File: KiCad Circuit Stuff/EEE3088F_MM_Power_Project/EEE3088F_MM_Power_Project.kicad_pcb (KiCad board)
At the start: 2 copper layers, 60 parts, among them J1 Conn_01x02, J2 Conn_02x16_Odd_Even, U1 MT3608, U2 INA219AIDCNR, U3 AMS1117-3.3, U4 TPS5430DDAR, U5 TP4056, U6 TS5A3159DCKR

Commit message: Connected All circuits, Ready for pcb design
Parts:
- added C13: 1uF, Capacitor_SMD:C_0402_1005Metric_Pad0.74x0.62mm_HandSolder, F.Cu at (167.0, 39.4)
- added C14: 10uF, Capacitor_SMD:C_0603_1608Metric_Pad1.08x0.95mm_HandSolder, F.Cu at (167.6, 53.5)
- added C17: 10uF, Capacitor_SMD:C_0603_1608Metric_Pad1.08x0.95mm_HandSolder, F.Cu at (167.6, 56.0)
- added C18: 220uF, Capacitor_SMD:C_Elec_6.3x7.7, F.Cu at (160.5, 42.5)
- added C19: 220uF, Capacitor_SMD:C_Elec_6.3x7.7, F.Cu at (160.5, 50.6)
- added C20: 220uF, Capacitor_SMD:C_Elec_6.3x7.7, F.Cu at (160.5, 58.8)
- added C21: 220uF, Capacitor_SMD:C_Elec_6.3x7.7, F.Cu at (160.5, 67.0)
- added C22: 100nF, Capacitor_SMD:C_0402_1005Metric_Pad0.74x0.62mm_HandSolder, F.Cu at (167.0, 41.4)
- added C23: 100nF, Capacitor_SMD:C_0402_1005Metric_Pad0.74x0.62mm_HandSolder, F.Cu at (167.0, 43.4)
- added C24: 220uF, Capacitor_SMD:C_Elec_6.3x7.7, F.Cu at (160.5, 75.1)
- added C25: 220uF, Capacitor_SMD:C_Elec_6.3x7.7, F.Cu at (160.5, 83.2)
- added C26: 100nF, Capacitor_SMD:C_0402_1005Metric_Pad0.74x0.62mm_HandSolder, F.Cu at (167.0, 45.3)
- added C27: 1uF, Capacitor_SMD:C_0402_1005Metric_Pad0.74x0.62mm_HandSolder, F.Cu at (167.0, 47.3)
- added C28: 1uF, Capacitor_SMD:C_0402_1005Metric_Pad0.74x0.62mm_HandSolder, F.Cu at (167.0, 49.3)
- added C29: 1uF, Capacitor_SMD:C_0402_1005Metric_Pad0.74x0.62mm_HandSolder, F.Cu at (167.0, 51.2)
- added C30: 220uF, Capacitor_SMD:C_Elec_6.3x7.7, F.Cu at (180.7, 43.0)
- added C31: 220uF, Capacitor_SMD:C_Elec_6.3x7.7, F.Cu at (180.7, 51.2)
- added C32: 100nF, Capacitor_SMD:C_0402_1005Metric_Pad0.74x0.62mm_HandSolder, F.Cu at (191.3, 62.0)
- added C33: 1uF, Capacitor_SMD:C_0402_1005Metric_Pad0.74x0.62mm_HandSolder, F.Cu at (191.3, 63.9)
- added R15: 75k, Resistor_SMD:R_0603_1608Metric_Pad0.98x0.95mm_HandSolder, F.Cu at (167.6, 58.5)
- added R16: 10k, Resistor_SMD:R_0603_1608Metric_Pad0.98x0.95mm_HandSolder, F.Cu at (167.6, 61.0)
- added SW1: SSSS810701, JLCPCB:SW-SMD_SSSS810701, F.Cu at (179.8, 56.8)
- added U10: DRV8833PWP, JLCPCB:TSSOP-16_L5.0-W4.4-P0.65-LS6.4-BL-EP, F.Cu at (213.5, 62.1)
- added U11: SS-12D06-G050, JLCPCB:SW-TH_3P-P4.70_SS-12D06-G050, F.Cu at (213.8, 35.0)
- added U12: AP22814AW5-7, JLCPCB:SOT-25_L3.0-W1.6-P0.95-LS2.8-BL, F.Cu at (188.1, 58.7)
- added U13: AP22814AW5-7, JLCPCB:SOT-25_L3.0-W1.6-P0.95-LS2.8-BL, F.Cu at (192.6, 58.7)
- added U14: AP22814AW5-7, JLCPCB:SOT-25_L3.0-W1.6-P0.95-LS2.8-BL, F.Cu at (197.1, 58.7)
- added U7: TYPE-C_16P_QTGM027, JLCPCB:USB-C-SMD_TYPE-C-16P-QTGM027, F.Cu at (192.5, 42.3)
- added U8: DRV8833PWP, JLCPCB:TSSOP-16_L5.0-W4.4-P0.65-LS6.4-BL-EP, F.Cu at (189.4, 52.1)
- added U9: HUSB237-AA001-DN06R, JLCPCB:TDFN-6_L2.0-W2.0-P0.65-TL-EP, F.Cu at (188.0, 62.8)
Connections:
- J2 pad 1: unconnected-(J2-Pin_1-Pad1) -> /BOUT2 (U1)
- J2 pad 10: unconnected-(J2-Pin_10-Pad10) -> /BIN2 (U2)
- J2 pad 11: unconnected-(J2-Pin_11-Pad11) -> /EXT_LOAD2_OUT
- J2 pad 2: unconnected-(J2-Pin_2-Pad2) -> /BOUT1 (U1)
- J2 pad 21: unconnected-(J2-Pin_21-Pad21) -> /EXT_LOAD1_OUT
- J2 pad 24: unconnected-(J2-Pin_24-Pad24) -> /AIN1 (U2)
- J2 pad 25: unconnected-(J2-Pin_25-Pad25) -> /CTRL_EXT_LOAD1
- J2 pad 26: unconnected-(J2-Pin_26-Pad26) -> /AIN2 (U2)
- J2 pad 27: unconnected-(J2-Pin_27-Pad27) -> /AOUT1 (U2)
- J2 pad 28: unconnected-(J2-Pin_28-Pad28) -> /AIN1 (U1)
- J2 pad 29: unconnected-(J2-Pin_29-Pad29) -> /AOUT2 (U2)
- J2 pad 3: unconnected-(J2-Pin_3-Pad3) -> /BOUT1 (U2)
- J2 pad 30: unconnected-(J2-Pin_30-Pad30) -> /AIN2 (U1)
- J2 pad 31: unconnected-(J2-Pin_31-Pad31) -> /AOUT2 (U1)
- J2 pad 32: unconnected-(J2-Pin_32-Pad32) -> /AOUT1 (U1)
- J2 pad 4: unconnected-(J2-Pin_4-Pad4) -> /BIN1 (U1)
- J2 pad 5: unconnected-(J2-Pin_5-Pad5) -> /BOUT2 (U2)
- J2 pad 6: unconnected-(J2-Pin_6-Pad6) -> /BIN2 (U1)
- J2 pad 7: unconnected-(J2-Pin_7-Pad7) -> /CTRL_EXT_LOAD2
- J2 pad 8: unconnected-(J2-Pin_8-Pad8) -> /BIN1 (U2)

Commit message: Got rid of old switch
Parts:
- removed C18, C19, C24, C25: 220uF, Capacitor_SMD:C_Elec_6.3x7.7
- removed C22, C26: 100nF, Capacitor_SMD:C_0402_1005Metric_Pad0.74x0.62mm_HandSolder
- removed C27, C29: 1uF, Capacitor_SMD:C_0402_1005Metric_Pad0.74x0.62mm_HandSolder
- removed R16: 10k, Resistor_SMD:R_0603_1608Metric_Pad0.98x0.95mm_HandSolder
- removed SW1: SSSS810701, JLCPCB:SW-SMD_SSSS810701
- removed U13: AP22814AW5-7, JLCPCB:SOT-25_L3.0-W1.6-P0.95-LS2.8-BL

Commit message: Added something
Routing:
- net GND: track 0.00 -> 27.0 mm
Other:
- board text added: "Hello Alex, Can you see this"
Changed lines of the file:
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@@
   )
   (setup
+    (stackup
+      (layer "F.SilkS" (type "Top Silk Screen"))
+      (layer "F.Paste" (type "Top Solder Paste"))
+      (layer "F.Mask" (type "Top Solder Mask") (thickness 0.01))
+      (layer "F.Cu" (type "copper") (thickness 0.035))
+      (layer "dielectric 1" (type "core") (thickness 1.51) (material "FR4") (epsilon_r 4.5) (loss_tangent 0.02))
+      (layer "B.Cu" (type "copper") (thickness 0.035))
+      (layer "B.Mask" (type "Bottom Solder Mask") (thickness 0.01))
+      (layer "B.Paste" (type "Bottom Solder Paste"))
+      (layer "B.SilkS" (type "Bottom Silk Screen"))
+      (copper_finish "None")
+      (dielectric_constraints no)
+    )
     (pad_to_mask_clearance 0)
     (pcbplotparams
@@
   (gr_rect (start 100 100) (end 177.3 152.95)
     (stroke (width 0.2) (type default)) (fill none) (layer "F.Cu"))
+  (gr_text "Hello Alex, Can you see this" (at 143.5 107.25) (layer "F.SilkS")
+    (effects (font (size 1.5 1.5) (thickness 0.3) bold) (justify left bottom mirror))
+  )
+  (segment (start 129.46 151) (end 134.54 151) (width 0.25) (layer "B.Cu") (net 4))
+  (segment (start 111.25 150.25) (end 112 151) (width 0.25) (layer "B.Cu") (net 4))
+  (segment (start 134.54 151) (end 135.75 149.79) (width 0.25) (layer "B.Cu") (net 4))
+  (segment (start 129.46 151) (end 130.67 149.79) (width 0.25) (layer "B.Cu") (net 4))
+  (segment (start 112 151) (end 129.46 151) (width 0.25) (layer "B.Cu") (net 4))
 )

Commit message: Done Significant circuit work
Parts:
- added C11: 2.2uF, Capacitor_SMD:C_0402_1005Metric_Pad0.74x0.62mm_HandSolder, F.Cu at (144.2, 134.9)
- added C12: 10nF, Capacitor_SMD:C_0402_1005Metric_Pad0.74x0.62mm_HandSolder, F.Cu at (146.0, 135.5)
- added C15: 2.2uF, Capacitor_SMD:C_0402_1005Metric_Pad0.74x0.62mm_HandSolder, F.Cu at (153.6, 134.7)
- added C16: 10nF, Capacitor_SMD:C_0402_1005Metric_Pad0.74x0.62mm_HandSolder, F.Cu at (155.3, 135.3)
- R1: footprint Resistor_SMD:R_0402_1005Metric_Pad0.72x0.64mm_HandSolder -> Resistor_SMD:R_1206_3216Metric_Pad1.30x1.75mm_HandSolder
- moved U11 146.4 mm to (110.0, 138.2), turned to -90 degrees
- moved U7 107.6 mm to (169.1, 147.3)
- moved U8 98.2 mm to (145.2, 139.8)
- moved U10 97.4 mm to (154.6, 139.6)
- moved CHRG_SelectR2_TP1 95.5 mm to (175.3, 116.6)
- moved CHRG_SelectR2_TP2 90.4 mm to (175.3, 113.1)
- moved C8 88.9 mm to (172.6, 129.2)
- moved R15 84.7 mm to (174.5, 142.9), turned to -90 degrees
- moved CHRG_SelectR1_TP1 82.6 mm to (168.1, 116.9)
- moved U6 80.1 mm to (172.5, 119.8), turned to 180 degrees
- moved D2 80.0 mm to (172.6, 133.9), turned to 90 degrees
- moved U9 79.9 mm to (171.4, 141.0), turned to 90 degrees
- moved C10 78.7 mm to (158.8, 129.6), turned to -90 degrees
- moved CHRG_SelectR1_TP2 78.6 mm to (168.1, 113.3)
- moved R9 77.1 mm to (171.9, 116.6), turned to 90 degrees
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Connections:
- C1 pad 1: /Battery_Out_After_Switch -> /Battery_Out
- C14 pad 1: /Battery_Out_After_Switch -> /Battery_Out
- C17 pad 1: /Battery_Out_After_Switch -> /Battery_Out
- C9 pad 2: /Battery_Out_Before_Switch -> /Battery_Out
- J1 pad 1: /Battery_In -> /Battery_In_Before_Switch
- J2 pad 14: /Battery_In -> /Battery_Out
- JP1 pad 1: /Battery_In -> /Battery_In_After_Switch
- JP2 pad 2: /Battery_Out_Before_Switch -> /Battery_Out
- L1 pad 1: /Battery_Out_After_Switch -> /Battery_Out
- L_TP_1 pad 1: /Battery_Out_After_Switch -> /Battery_Out
- R1 pad 1: /Battery_Out_Before_Switch -> /Battery_Out
- R1 pad 2: /Battery_In -> /Battery_In_After_Switch
- R5 pad 1: /Battery_In -> /Battery_In_After_Switch
- R6 pad 1: /Battery_Out_Before_Switch -> /Battery_Out
- Shunt_TP1 pad 1: /Battery_In -> /Battery_In_After_Switch
- Shunt_TP2 pad 1: /Battery_Out_Before_Switch -> /Battery_Out
- U1 pad 4: /Battery_Out_After_Switch -> /Battery_Out
- U1 pad 5: /Battery_Out_After_Switch -> /Battery_Out
- U10 pad 12: /Battery_Out_After_Switch -> /Battery_Out
- U10 pad 16: /AIN2 (U2) -> /AIN1 (U2)
- U11 pad 1: /Battery_Out_After_Switch -> /Battery_In_After_Switch
- U11 pad 2: /Battery_Out_Before_Switch -> /Battery_In_Before_Switch
- U5 pad 5: /Battery_Out_Before_Switch -> /Battery_Out
- U6 pad 5: +5V -> /Battey_Charger_VDD
- U7 pad A6: /DP2 -> /DP1
- U7 pad A7: /DN2 -> /DN1
- U8 pad 12: /Battery_Out_After_Switch -> /Battery_Out
- U9 pad 4: /DP1/DP2 -> /DP1
- U9 pad 5: /DN1/DN2 -> /DN1
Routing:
- net /Battery_Out: track 0.00 -> 113.1 mm
- net GND: track 27.0 -> 110.1 mm, vias 0 -> 15
- net +3V3: track 0.00 -> 53.2 mm, vias 0 -> 2
- net /I2C1_SDA: track 0.00 -> 51.2 mm, vias 0 -> 1
- net +5V: track 0.00 -> 44.4 mm
- net /I2C1_SCL: track 0.00 -> 41.5 mm, vias 0 -> 1
- net /AOUT2 (U2): track 0.00 -> 39.9 mm
- net /AOUT1 (U2): track 0.00 -> 34.4 mm
- net /BOUT1 (U1): track 0.00 -> 27.2 mm, vias 0 -> 2
- net /BIN2 (U1): track 0.00 -> 26.2 mm, vias 0 -> 1
- net /BIN1 (U1): track 0.00 -> 25.7 mm, vias 0 -> 2
- net /Battey_Charger_VDD: track 0.00 -> 25.2 mm
- net /BOUT2 (U1): track 0.00 -> 24.3 mm, vias 0 -> 2
- net +9V: track 0.00 -> 20.1 mm
- net /BIN2 (U2): track 0.00 -> 16.8 mm, vias 0 -> 1
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- added copper zone on B.Cu, net GND

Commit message: Did somke more pcb
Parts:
- moved C6 80.8 mm to (167.7, 137.2)
- moved C7 66.5 mm to (155.5, 123.5), turned to -90 degrees
- moved C9 63.4 mm to (161.7, 119.1), turned to 180 degrees
- moved R7 59.3 mm to (157.9, 123.5)
- moved C31 58.9 mm to (158.0, 105.6)
- moved R8 57.8 mm to (157.9, 122.0)
- moved C3 48.3 mm to (123.4, 124.6), turned to -90 degrees
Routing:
- net +9V: track 20.1 -> 73.8 mm, vias 0 -> 4
- net +5V: track 44.4 -> 82.4 mm, vias 0 -> 2
- net +3V3: track 53.2 -> 88.1 mm, vias 2 -> 4
- net /AOUT1 (U1): track 0.00 -> 33.7 mm, vias 0 -> 1
- net /AOUT2 (U1): track 0.00 -> 32.6 mm, vias 0 -> 1
- net /AIN2 (U1): track 0.00 -> 25.9 mm, vias 0 -> 1
- net /AIN1 (U1): track 0.00 -> 24.3 mm, vias 0 -> 1
- net /Battery_Out: track 113.1 -> 133.4 mm, vias 0 -> 1
- net GND: track 110.1 -> 128.1 mm, vias 15 -> 16
- net /Battey_Charger_VDD: track 25.2 -> 29.6 mm
- net Net-(C7-Pad1): track 0.00 -> 3.63 mm
- net /AOUT1 (U2): track 34.4 -> 36.8 mm
- net /AOUT2 (U2): track 39.9 -> 41.2 mm

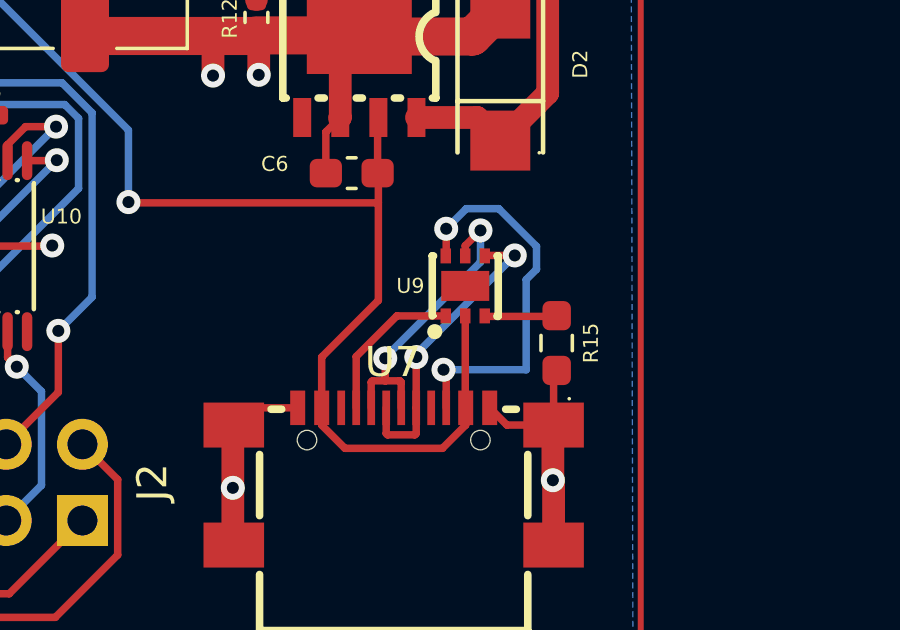
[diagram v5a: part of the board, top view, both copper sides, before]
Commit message: Removed D+ and D- to float on the USPD
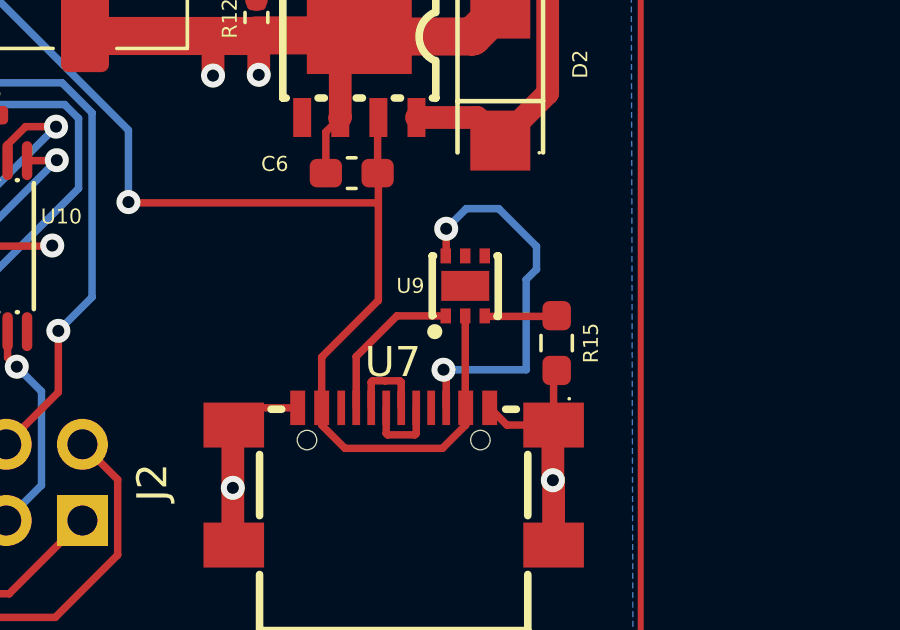
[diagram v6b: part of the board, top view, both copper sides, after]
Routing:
- net /DP1: track 10.2 -> 2.77 mm, vias 2 -> 0
- net /DN1: track 10.1 -> 2.75 mm, vias 2 -> 0
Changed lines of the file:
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@@
   (segment (start 169.314872 145.034) (end 169.314872 144.178869) (width 0.25) (layer "F.Cu") (net 57))
   (segment (start 169.314872 144.178869) (end 169.269997 144.133994) (width 0.25) (layer "F.Cu") (net 57))
-  (segment (start 171.958 139.120422) (end 171.449975 139.628447) (width 0.25) (layer "F.Cu") (net 57))
-  (segment (start 168.783 144.133994) (end 168.783 143.383) (width 0.25) (layer "F.Cu") (net 57))
   (segment (start 168.783 144.133994) (end 168.360003 144.133994) (width 0.25) (layer "F.Cu") (net 57))
   (segment (start 169.269997 144.133994) (end 168.783 144.133994) (width 0.25) (layer "F.Cu") (net 57))
-  (segment (start 171.449975 139.628447) (end 171.449975 139.969924) (width 0.25) (layer "F.Cu") (net 57))
   (segment (start 168.314872 144.179125) (end 168.314872 145.034) (width 0.25) (layer "F.Cu") (net 57))
   (segment (start 168.360003 144.133994) (end 168.314872 144.179125) (width 0.25) (layer "F.Cu") (net 57))
-  (via (at 171.958 139.120422) (size 0.8) (drill 0.4) (layers "F.Cu" "B.Cu") (net 57))
-  (via (at 168.783 143.383) (size 0.8) (drill 0.4) (layers "F.Cu" "B.Cu") (net 57))
-  (segment (start 168.783 143.383) (end 168.783 143.353167) (width 0.25) (layer "B.Cu") (net 57))
-  (segment (start 171.958 140.178167) (end 171.958 139.120422) (width 0.25) (layer "B.Cu") (net 57))
-  (segment (start 168.783 143.353167) (end 171.958 140.178167) (width 0.25) (layer "B.Cu") (net 57))
   (segment (start 168.859875 145.934006) (end 168.815 145.889131) (width 0.25) (layer "F.Cu") (net 58))
   (segment (start 168.815 145.889131) (end 168.815 145.034) (width 0.25) (layer "F.Cu") (net 58))
   (segment (start 172.115886 139.954) (end 172.099962 139.969924) (width 0.25) (layer "F.Cu") (net 58))
-  (segment (start 173.101 139.954) (end 172.115886 139.954) (width 0.25) (layer "F.Cu") (net 58))
-  (segment (start 169.815 143.346472) (end 169.81939 143.342082) (width 0.25) (layer "F.Cu") (net 58))
-  (segment (start 169.815 145.034) (end 169.815 143.346472) (width 0.25) (layer "F.Cu") (net 58))
   (segment (start 169.815 145.034) (end 169.815 145.888875) (width 0.25) (layer "F.Cu") (net 58))
   (segment (start 169.815 145.888875) (end 169.769869 145.934006) (width 0.25) (layer "F.Cu") (net 58))
   (segment (start 169.769869 145.934006) (end 168.859875 145.934006) (width 0.25) (layer "F.Cu") (net 58))
-  (via (at 169.81939 143.342082) (size 0.8) (drill 0.4) (layers "F.Cu" "B.Cu") (net 58))
-  (via (at 173.101 139.954) (size 0.8) (drill 0.4) (layers "F.Cu" "B.Cu") (net 58))
-  (segment (start 169.81939 143.342082) (end 169.81939 143.23561) (width 0.25) (layer "B.Cu") (net 58))
-  (segment (start 169.81939 143.23561) (end 173.101 139.954) (width 0.25) (layer "B.Cu") (net 58))
   (segment (start 170.815 139.954911) (end 170.799987 139.969924) (width 0.25) (layer "F.Cu") (net 60))
   (segment (start 170.815 143.853525) (end 170.725475 143.764) (width 0.25) (layer "F.Cu") (net 60))

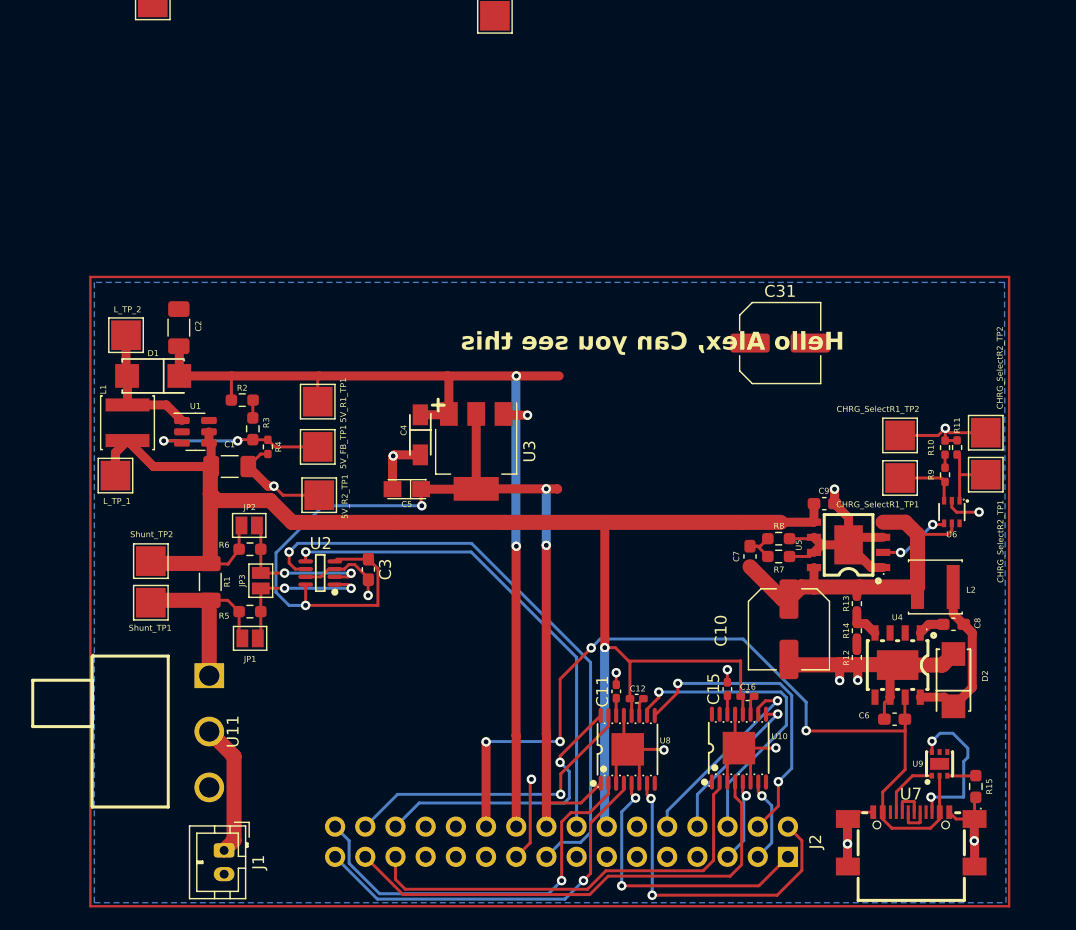
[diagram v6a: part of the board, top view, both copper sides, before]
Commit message: Changed inductors and rewired
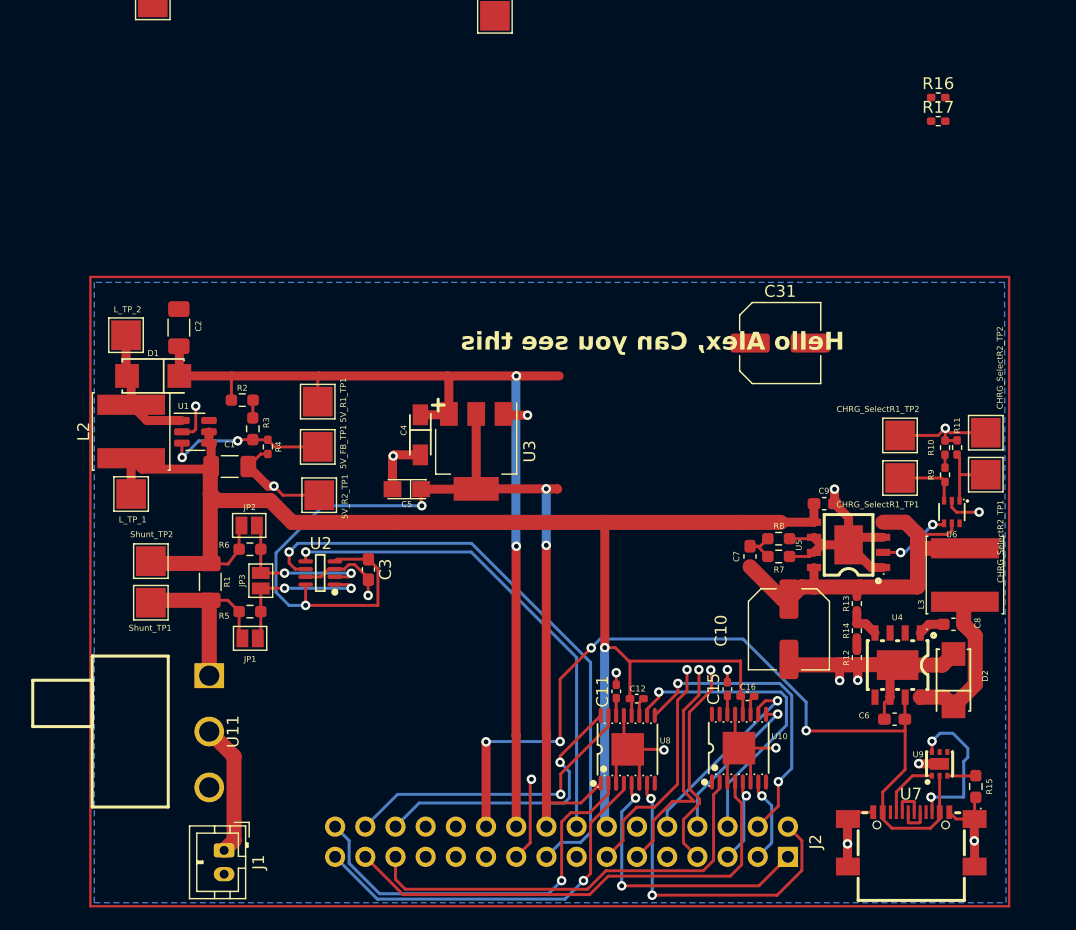
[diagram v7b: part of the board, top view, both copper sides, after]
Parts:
- removed L1: 10u, Inductor_SMD:L_Changjiang_FNR4030S
- added L3: 22u, Inductor_SMD:L_Sunlord_SWPA6045S, F.Cu at (173.6, 125.1)
- added R16: 3.3k, Resistor_SMD:R_0402_1005Metric_Pad0.72x0.64mm_HandSolder, F.Cu at (171.3, 84.9)
- added R17: 3.3k, Resistor_SMD:R_0402_1005Metric_Pad0.72x0.64mm_HandSolder, F.Cu at (171.3, 86.9)
- L2: value 18u -> 22u; footprint Inductor_SMD:L_Changjiang_FNR4030S -> Inductor_SMD:L_Sunlord_SWPA6045S
- R11: value 2k -> 2.2k
- moved L2 68.9 mm to (103.4, 113.0), turned to 90 degrees
- moved L_TP_1 2.04 mm to (103.4, 118.3)
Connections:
- L2 pad 1: /PH_Pin -> /Battery_Out
- L2 pad 2: /Battey_Charger_VDD -> Net-(D1-A)
- U9 pad 4: /DP1 -> unconnected-(U9-D+-Pad4)
- U9 pad 5: /DN1 -> unconnected-(U9-D--Pad5)
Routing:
- net /EXT_LOAD2_OUT: track 0.00 -> 19.7 mm, vias 0 -> 1
- net /Fast_Charge_CTRL: track 0.00 -> 19.4 mm, vias 0 -> 1
- net /CTRL_EXT_LOAD2: track 0.00 -> 17.9 mm, vias 0 -> 1
- net GND: track 128.1 -> 133.1 mm, vias 16 -> 18
- net /Battey_Charger_VDD: track 29.6 -> 33.7 mm
- net /PH_Pin: track 16.3 -> 13.1 mm
- net Net-(U1-FB): track 14.9 -> 13.5 mm
- net /Battery_Out: track 133.4 -> 132.3 mm
